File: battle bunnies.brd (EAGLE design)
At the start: 151.7 x 94 mm, 59 parts, among them IC1 CP2104, Q1 mmbt2222, Q2 mmbt2222, SW2 KMR2, U1 PCA9685, U2 SPX3819, U3 MCP73831T-2ACI/OT, X2 ESP-12, X4 20329

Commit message: more silk changes
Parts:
- RN2: value (none) -> 220
- RN3: value (none) -> 10K
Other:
- board text added: "This is intended as a fun badge toy to play with. This version was designed for PyCon Pune India, February 2017. Go, play with others and see what comes of it! - John & Terri"
- board text removed: "This is intended as a fun badge toy to play with. It was designed for PyCon Pune India, February 2017. Go, play with others and see what comes of it! - John & Terri"
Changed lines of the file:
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@@
 <setting verticaltext="up"/>
 </settings>
-<grid distance="0.05" unitdist="inch" unit="inch" style="lines" multiple="1" display="yes" altdistance="0.0125" altunitdist="inch" altunit="inch"/>
+<grid distance="0.05" unitdist="inch" unit="mm" style="lines" multiple="1" display="yes" altdistance="0.0125" altunitdist="inch" altunit="mm"/>
 <layers>
 <layer number="1" name="Top" color="4" fill="1" visible="yes" active="yes"/>
@@
 <text x="80.01" y="83.82" size="2.54" layer="22" rot="MR270">Battle Bunnies v0.9</text>
 <text x="53.34" y="77.47" size="1.016" layer="22" rot="MR270">This is intended as a fun badge toy to play with.
-It was designed for PyCon Pune India, February 2017.
+This version was designed for
+PyCon Pune India, February 2017.
 Go, play with others and see what comes of it!
 - John &amp; Terri</text>
@@
 <attribute name="OC_NEWARK" value="unknown" x="102.87" y="67.31" size="1.016" layer="28" font="vector" rot="MR90" display="off"/>
 </element>
-<element name="RN2" library="resistor-dil" package="EXB2HV" value="" x="102.87" y="57.4675" rot="MR90">
+<element name="RN2" library="resistor-dil" package="EXB2HV" value="220" x="102.87" y="57.4675" rot="MR90">
 <attribute name="OC_NEWARK" value="unknown" x="102.87" y="57.4675" size="0.17018125" layer="28" rot="MR90" display="off"/>
 <attribute name="MPN" value="" x="102.87" y="57.4675" size="0.17018125" layer="28" rot="MR90" display="off"/>
@@
 <attribute name="MF" value="" x="102.87" y="57.4675" size="0.17018125" layer="28" rot="MR90" display="off"/>
 </element>
-<element name="RN3" library="resistor-dil" package="EXB2HV" value="" x="89.8525" y="69.215" rot="MR0">
+<element name="RN3" library="resistor-dil" package="EXB2HV" value="10K" x="89.8525" y="69.215" rot="MR0">
 <attribute name="OC_NEWARK" value="unknown" x="89.8525" y="69.215" size="0.17018125" layer="28" rot="MR0" display="off"/>
 <attribute name="MPN" value="" x="89.8525" y="69.215" size="0.17018125" layer="28" rot="MR0" display="off"/>

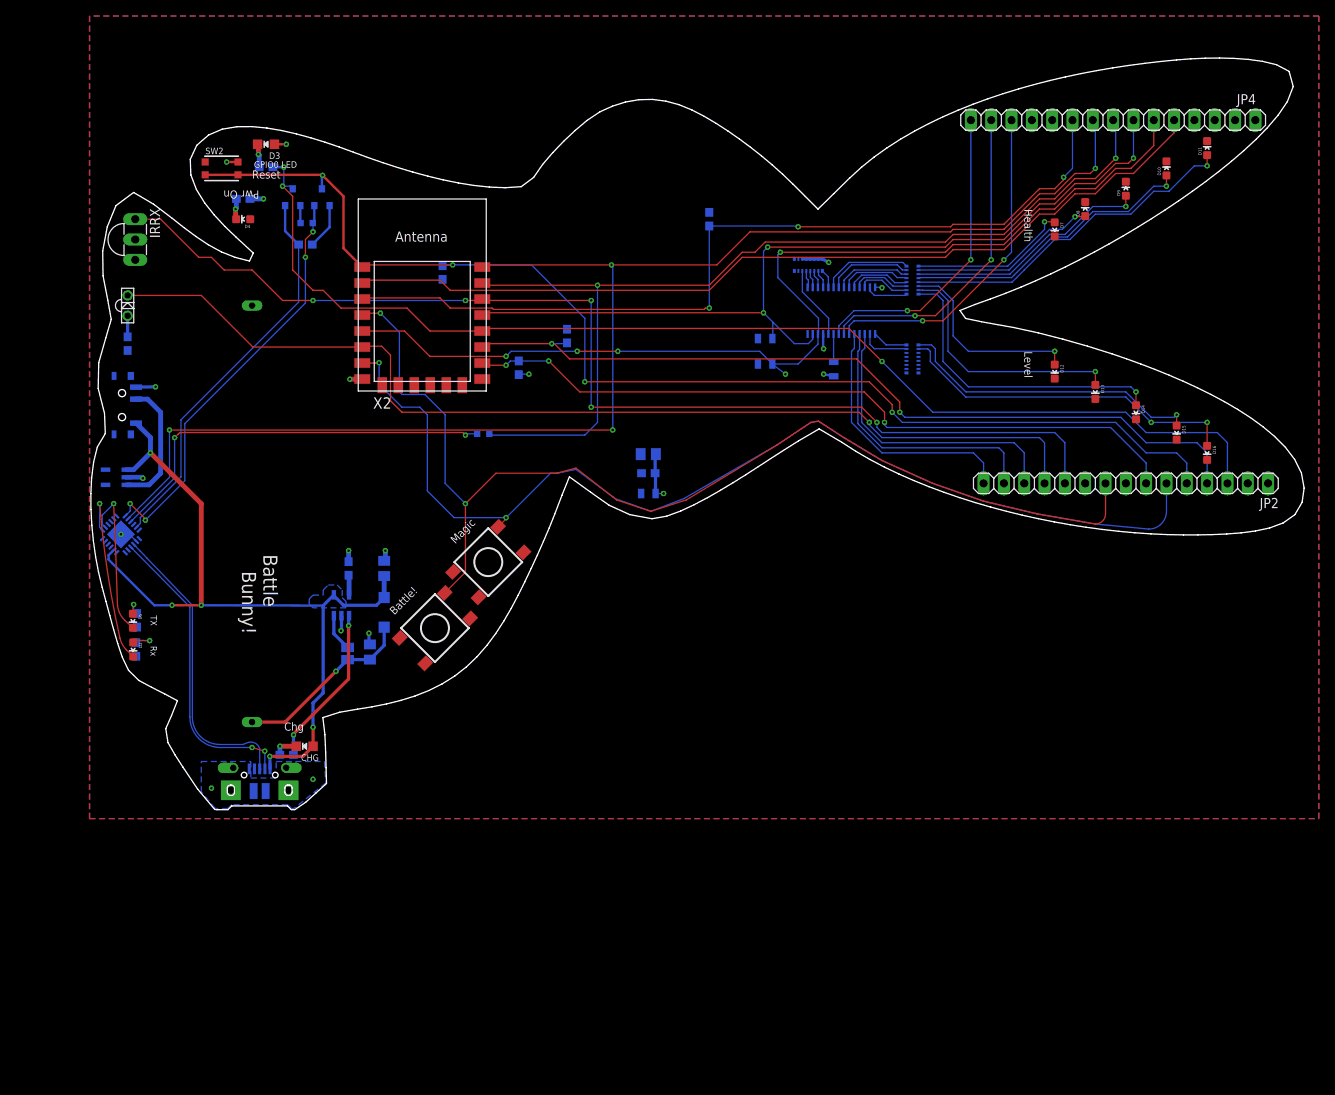
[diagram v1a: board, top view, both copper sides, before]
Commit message: Initial sensor board work
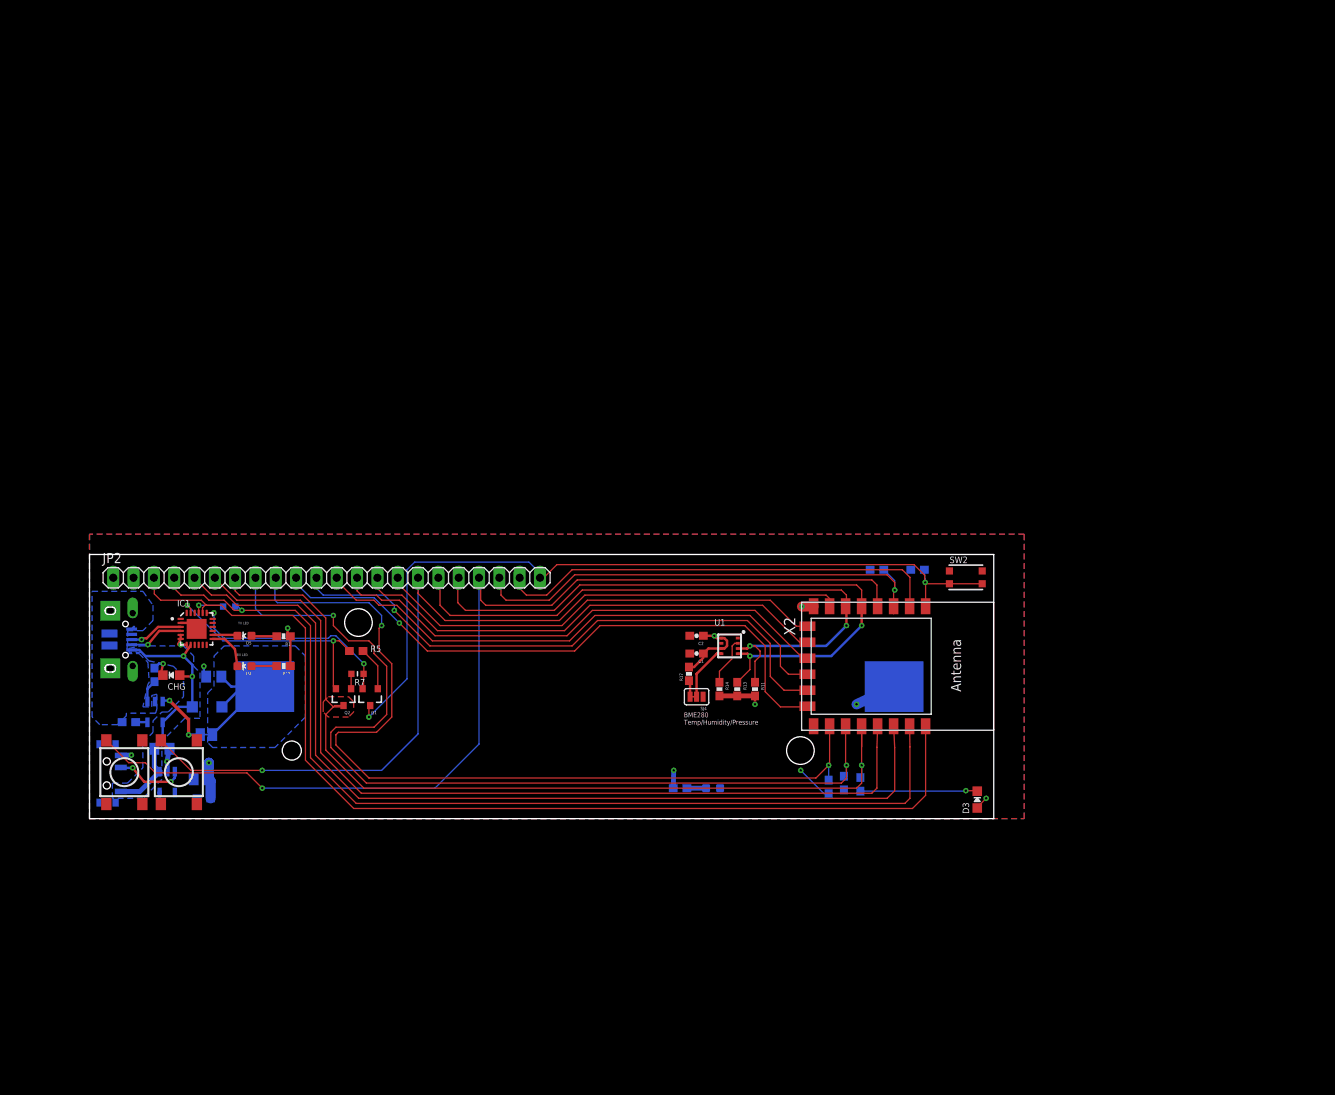
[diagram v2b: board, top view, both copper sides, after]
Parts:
- removed D10, D12, D13, D14, D15, D7, D8, D9: GREEN, SparkFun-LED:LED-0603
- removed D11, D16: RED, SparkFun-LED:LED-0603
- removed D6: (no value), SparkFun-LED:LTE-302
- removed IRRX: TSOP38, Opto-electronics:TSOP38
- removed JP4: (no value), pinhead:1X15
- removed R20, R21, R22: 10K, SparkFun-Passives:0805
- removed R23: 270, microbuilder:0603-NO
- removed RN1, RN2: 220, resistor-dil:EXB2HV
- removed RN3: 10K, resistor-dil:EXB2HV
- added C2: 0.1uF, SparkFun-Capacitors:0603-CAP
- added R11, R13, R14, R17: 4.7K, SparkFun-Resistors:0603-RES
- added SJ4: EN ADR PULLUP, SparkFun-Passives:PAD-JUMPER-3-2OF3_NC_BY_TRACE_YES_SILK_FULL_BOX
- C1: value 10uF -> 0.1uF; device SparkFun-Capacitors:0805-CAP -> SparkFun-Capacitors:0603-CAP
- JP2: device pinhead:1X15 -> pinhead:1X22
- U$31: value AA1 -> 18650; device Electromechanical:AA1 -> Warthog9-Batteries:KEYSTONE1042
- U1: value PCA9685 -> BME280; device microbuilder:TSSOP28 -> BME280ComponentLibrary:BME280_LGA
- moved D3 120.9 mm to (111.0, 2.38), turned to 0 degrees
- moved R10 107.1 mm to (96.4, 4.29), turned to 270 degrees
- moved SW2 106.1 mm to (109.5, 30.2)
- moved JP2 100.6 mm to (29.6, 30.1), turned to 0 degrees
- moved D4 92.2 mm to (77.9, 3.81), flipped to the bottom, turned to 270 degrees
- moved R16 91.7 mm to (73.8, 3.81), turned to 0 degrees
- moved X2 72.2 mm to (98.7, 19.1), turned to 270 degrees
- moved R4 70.0 mm to (103.5, 31.1), turned to 0 degrees
- moved C8 69.1 mm to (14.0, 4.92)
- moved C7 68.8 mm to (14.3, 2.54)
- moved R9 65.7 mm to (94.3, 4.45), turned to 270 degrees
- moved R6 65.2 mm to (92.4, 3.97)
- moved Q2 62.7 mm to (31.8, 15.2), flipped to the top, turned to 180 degrees
- moved Q1 62.7 mm to (35.1, 15.2), flipped to the top, turned to 180 degrees
- moved R7 56.7 mm to (33.5, 18.1), flipped to the top, turned to 180 degrees
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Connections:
- removed net A0: RN3.5, U1.1
- removed net A1: RN3.4, U1.2
- removed net A2: RN3.3, U1.3
- removed net A3: RN3.2, U1.4
- removed net A4: RN3.1, U1.5
- removed net A5: RN3.6, U1.24
- removed net N$14: D6.A, R23.1
- removed net N$16: D14.A, RN1.16
- removed net N$17: D12.A, RN1.14
- removed net N$18: D11.A, RN1.13
- removed net N$19: D10.A, RN1.12
- removed net N$20: D9.A, RN1.11
- removed net N$21: D8.A, RN1.10
- removed net N$22: D7.A, RN1.9
- removed net N$23: D15.A, RN2.9
- removed net N$24: D16.A, RN2.10
- removed net OE: R20.1, U1.23
- removed net PWM0: RN1.8, U1.6
- removed net PWM1: RN1.7, U1.7
- removed net PWM10: JP2.13, U1.17
- removed net PWM11: JP2.14, U1.18
- removed net PWM12: JP2.15, U1.19
- removed net PWM13: JP4.13, U1.20
- removed net PWM14: JP4.14, U1.21
- removed net PWM15: JP4.15, U1.22
- removed net PWM2: RN1.6, U1.8
- removed net PWM3: RN1.5, U1.9
- removed net PWM4: RN1.4, U1.10
- removed net PWM5: RN1.3, U1.11
- removed net PWM6: RN1.2, U1.12
- removed net PWM7: RN1.1, U1.13
- removed net PWM8: RN2.8, U1.15
- removed net PWM9: RN2.7, U1.16
- new net !CS: R14.1, U1.P$2
- new net CLK: JP2.12, X2.20
- new net CS: JP2.15, X2.17
- new net DI: JP2.11, X2.21
- new net DO: JP2.14, X2.18
- new net GPIO10: JP2.13, X2.19
- new net GPIO9: JP2.10, X2.22
- new net SDO/ADR: SJ4.2, U1.P$5
- net 3.3V: now also C2.1, R11.2, R13.2, R14.2, R17.2, U1.P$6, U1.P$8; no longer IRRX.3, JP4.1, R21.2, R22.2, R23.2, U1.28
- net ADC: now also JP2.21; no longer JP4.5
- net CH_PD: now also JP2.20; no longer JP4.10
- net GND: now also C2.2, SJ4.1, U1.P$1, U1.P$7; no longer D10.C, D11.C, D12.C, D13.C, D14.C, D15.C, D16.C, D7.C, D8.C, D9.C, IRRX.2, JP4.2, R20.2, RN3.11, RN3.12, RN3.13, RN3.14, RN3.15, RN3.16, U1.14, U1.25
- net GPIO0: now also JP2.7; no longer JP2.3
- net GPIO12/MISO: now also JP2.17, R11.1, U1.P$3; no longer D6.C, JP2.12
- net GPIO13/MOSI: now also JP2.16; no longer JP2.6
- net GPIO14/SCK: now also JP2.18, R13.1, U1.P$4; no longer JP4.6, R22.1, U1.26
- net GPIO15: now also JP2.9; no longer JP2.7
- net GPIO16: now also JP2.19; no longer JP2.9
- net GPIO2: now also JP2.8; no longer JP2.4
- net GPIO4/SDA: now also JP2.6; no longer JP4.7, R21.1, U1.27
- net GPIO5/SCL: now also JP2.5; no longer IRRX.1, JP2.11
- net N$15: now also R17.1, SJ4.3; no longer D13.A, RN1.15
- net RESET: now also JP2.22; no longer JP2.5
- net RXD: now also JP2.4; no longer JP4.8
- net TXD: now also JP2.3; no longer JP4.9
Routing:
- net GPIO9: track 0.00 -> 77.0 mm, vias 0 -> 1
- net DI: track 0.00 -> 73.4 mm, vias 0 -> 1
- net CLK: track 0.00 -> 68.2 mm
- net GPIO10: track 0.00 -> 64.1 mm
- net VBUS: track 98.2 -> 34.5 mm, vias 5 -> 2
- net DO: track 0.00 -> 60.5 mm
- net CS: track 0.00 -> 56.8 mm
- net ADC: track 111.9 -> 55.8 mm
- net RESET: track 153.2 -> 102.1 mm, vias 4 -> 2
- net GPIO14/SCK: track 131.4 -> 81.2 mm, vias 5 -> 2
- net GPIO12/MISO: track 130.9 -> 81.7 mm, vias 1 -> 2
- net CH_PD: track 109.0 -> 60.6 mm, vias 3 -> 1
- net TXD: track 177.3 -> 129.8 mm, vias 4 -> 0
- net USB_RX: track 51.0 -> 4.07 mm, vias 2 -> 1
- net N$24: track 43.9 -> 0.00 mm, vias 2 -> 0
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- added copper zone on layer 1, net GPIO0
- added copper zone on layer 16, net VBAT
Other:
- board size 151.7 x 94 mm -> 113 x 33 mm
- board text added: "BME280 Temp/Humidity/Pressure"
- board text added: "RX LED"
- board text added: "TX LED"
- board text removed: "(C) John 'Warthog9' Hawley 2016 CC-BY-SA Artwork by Dr. Terri Oda"
- board text removed: "3.3V"
- board text removed: "ADC"
- board text removed: "Battle Bunnies v0.9"
- board text removed: "Battle Bunny!"
- board text removed: "Battle!"
- board text removed: "CH_PD"
- board text removed: "Chg"
- board text removed: "GND"
- board text removed: "GPIO0"
- board text removed: "GPIO0 LED"
- board text removed: "GPIO12"
- board text removed: "GPIO13"
- board text removed: "GPIO14"
- board text removed: "GPIO15"
- board text removed: "GPIO16"
- board text removed: "GPIO2"
- board text removed: "GPIO4"
- board text removed: "GPIO5"
- board text removed: "Health"
- board text removed: "Level"
- board text removed: "Magic"
- board text removed: "PWM10"
- board text removed: "PWM11"
- board text removed: "PWM12"
- board text removed: "PWM13"
- board text removed: "PWM14"
- board text removed: "PWM15"
- board text removed: "Pwr On"
- board text removed: "RESET"
- board text removed: "RXD"
- board text removed: "Reset"
- board text removed: "Rx"
- board text removed: "TX"
- board text removed: "TXD"
- board text removed: "This is intended as a fun badge toy to play with. This version was designed for PyCon Pune India, February 2017. Go, play with others and see what comes of it! - John & Terri"

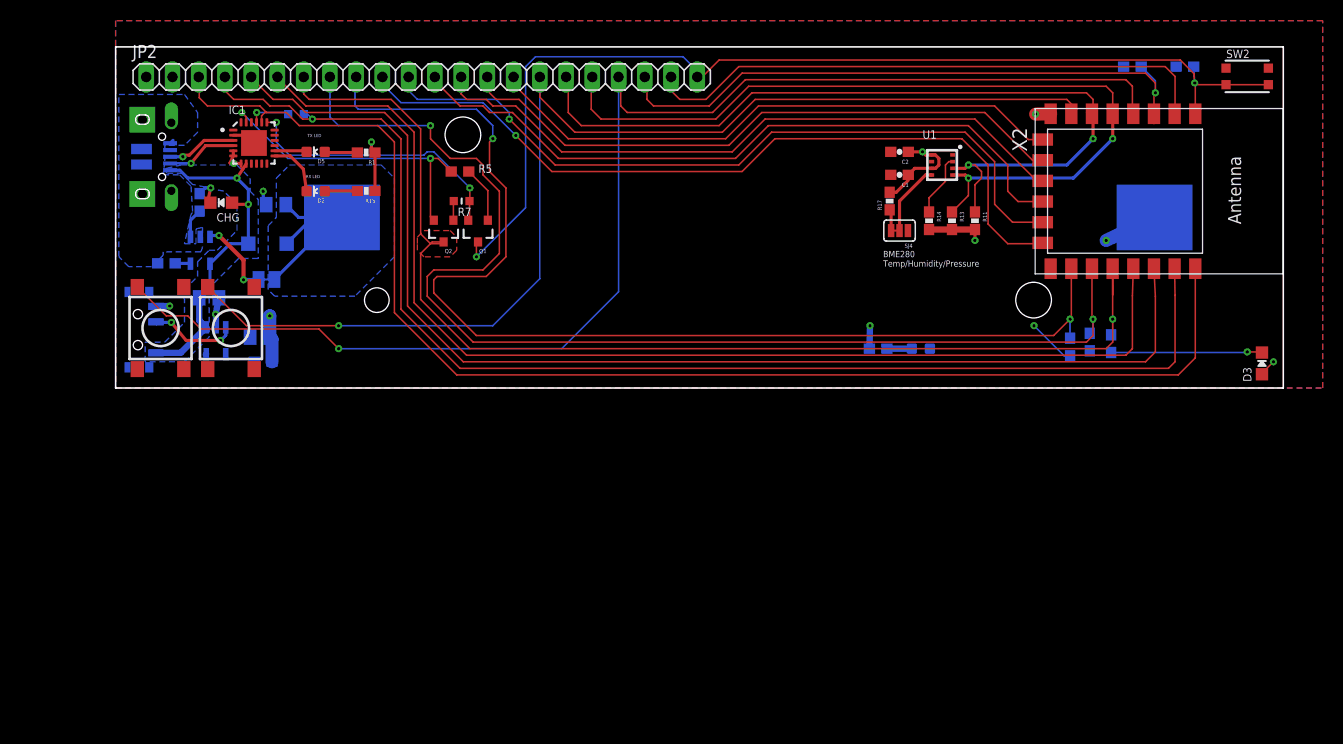
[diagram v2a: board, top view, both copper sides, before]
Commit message: Initial commit for ESP32 conversion
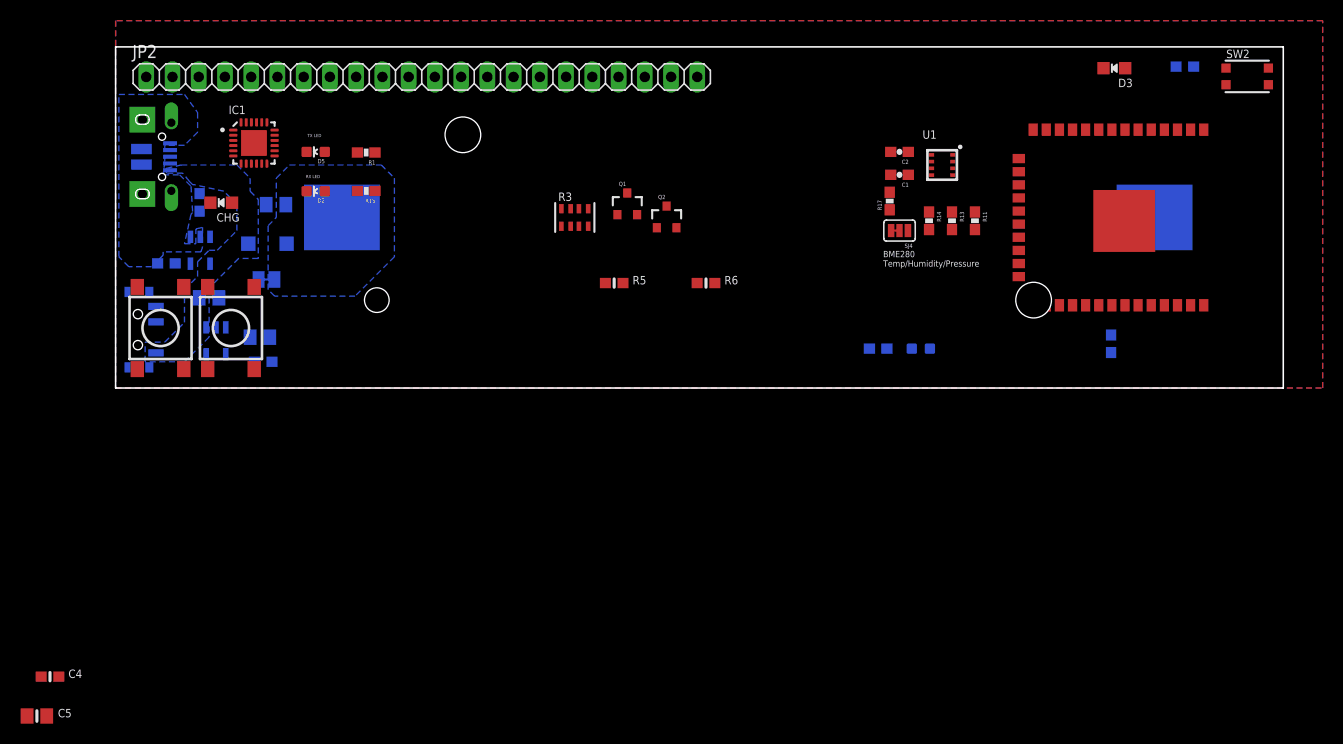
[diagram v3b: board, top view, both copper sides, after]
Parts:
- removed R12: 1K, microbuilder:_0603MP
- removed R7: 10K, microbuilder:_0603MP
- removed R9: 10K, microbuilder:0603-NO
- added C4: 1uF, microbuilder:0603-NO
- added C5: 10uF, microbuilder:0805-NO
- R3: device microbuilder:0603-NO -> microbuilder:RESPACK_4X0603
- R5: value 10K -> 100K
- R6: value 4.7K -> 100K
- X2: value ESP-12 -> ESP32_WROOM32_SKINNY; device microbuilder:ESP-12E -> microbuilder:WROOM32_SKINNY
- moved R3 55.9 mm to (44.5, 16.5), flipped to the top
- moved R6 35.8 mm to (57.1, 10.2), flipped to the top, turned to 0 degrees
- moved D3 31.9 mm to (96.7, 31.0), turned to 90 degrees
- moved Q2 21.6 mm to (53.3, 16.5), turned to 0 degrees
- moved R5 18.4 mm to (48.3, 10.2)
- moved Q1 14.7 mm to (49.5, 17.8), turned to 0 degrees
- moved X2 3.00 mm to (100.3, 16.5)
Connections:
- new net A0_DAC2: X2.11
- new net A13_I35: R5.1, R6.2, X2.7
- new net A1_DAC1: X2.10
- new net A2_I34: X2.6
- new net A3_I39: X2.5
- new net A4_IO36: X2.4
- new net A5_IO4: X2.26
- new net IO12_A11: X2.14
- new net IO13_A12: X2.16
- new net IO14_A6: X2.13
- new net IO15_A8: X2.23
- new net IO16: X2.27
- new net IO17: X2.28
- new net IO21: X2.33
- new net IO27_A10: X2.12
- new net IO32_A7: X2.8
- new net IO33_A9: X2.9
- new net MISO: X2.31
- new net MOSI: X2.30
- new net RXD0: X2.34
- new net SCK: X2.29
- new net SCL: X2.36
- new net SDA: X2.37
- new net TXD0: X2.35
- net 3.3V: now also C5.1, X2.2; no longer R3.2, R9.2, X2.8
- net ADC: no longer X2.2
- net CH_PD: no longer R3.1, X2.3
- net CLK: no longer X2.20
- net CS: no longer X2.17
- net DI: no longer X2.21
- net DO: no longer X2.18
- net DTR: now also R3.4; no longer R5.1
- net GND: now also C4.2, C5.2, X2.1, X2.15, X2.38, X2.P$1; no longer X2.9
- net GPIO0: now also X2.25; no longer X2.12
- net GPIO10: no longer X2.19
- net GPIO12/MISO: no longer X2.6
- net GPIO13/MOSI: no longer X2.7
- net GPIO14/SCK: no longer X2.5
- net GPIO15: no longer R6.2, X2.10
- net GPIO16: no longer X2.4
- net GPIO2: now also X2.24; no longer R9.1, X2.11
- net GPIO4/SDA: no longer X2.13
- net GPIO5/SCL: no longer X2.14
- net GPIO9: no longer X2.22
- net N$12: now also R3.5; no longer R5.2
- net N$13: now also R3.2; no longer R7.2
- net RESET: now also C4.1, X2.3; no longer X2.1
- net RTS: now also R3.7; no longer R7.1
- net RXD: no longer R12.2, X2.15
- net TXD: no longer X2.16
- net USB_RX: no longer R12.1
- net VBAT: now also R5.2
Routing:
- net TXD: track 129.8 -> 0.00 mm
- net GPIO16: track 129.1 -> 0.00 mm, vias 1 -> 0
- net RXD: track 124.4 -> 0.00 mm, vias 1 -> 0
- net GPIO5/SCL: track 117.1 -> 0.00 mm
- net GPIO2: track 115.0 -> 0.00 mm, vias 2 -> 0
- net GPIO0: track 114.8 -> 0.00 mm, vias 1 -> 0
- net GPIO13/MOSI: track 112.5 -> 0.00 mm, vias 1 -> 0
- net GPIO4/SDA: track 111.6 -> 0.00 mm
- net GPIO15: track 110.4 -> 0.00 mm, vias 2 -> 0
- net RESET: track 102.1 -> 0.00 mm, vias 2 -> 0
- net GPIO12/MISO: track 81.7 -> 0.00 mm, vias 2 -> 0
- net GPIO14/SCK: track 81.2 -> 0.00 mm, vias 2 -> 0
- net GPIO9: track 77.0 -> 0.00 mm, vias 1 -> 0
- net DI: track 73.4 -> 0.00 mm, vias 1 -> 0
- net CLK: track 68.2 -> 0.00 mm
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- removed copper zone on layer 1, net GPIO0
